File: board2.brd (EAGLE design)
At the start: 100 x 80 mm, 76 parts, among them Q1 7.68M, Q2 16MHz

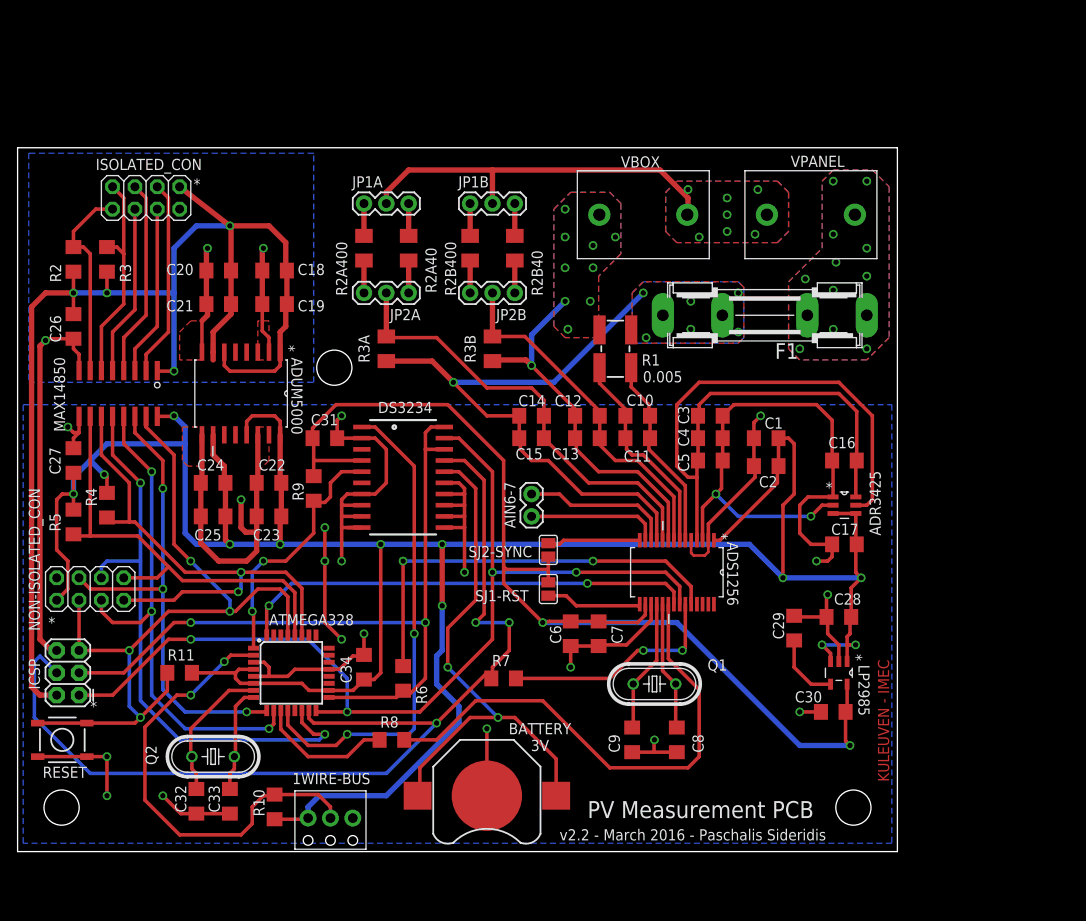
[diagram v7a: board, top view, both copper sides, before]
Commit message: Visual changes and clean up
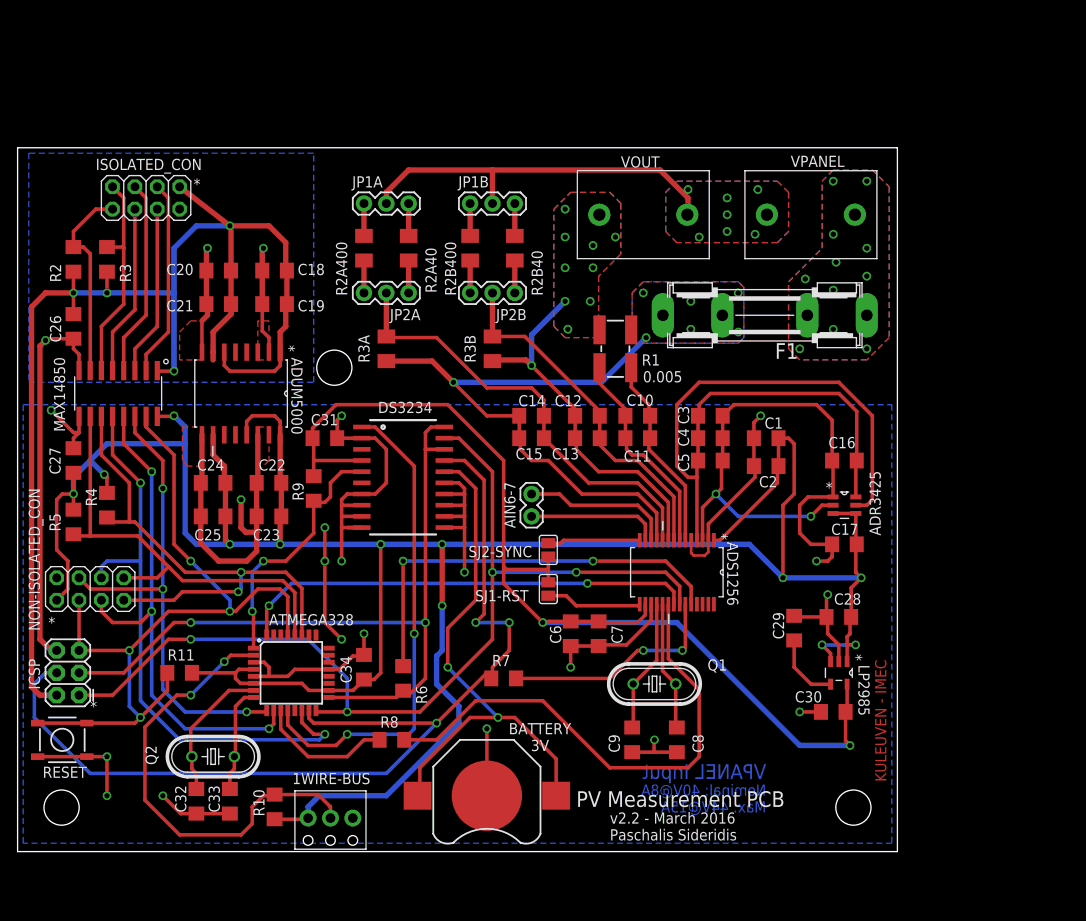
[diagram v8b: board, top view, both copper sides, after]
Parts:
- renumbered VBOX to VOUT
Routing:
- net MOSI: track 118.2 -> 115.2 mm
- net GND_ISO: track 269.9 -> 272.6 mm
- net AIN5: track 68.9 -> 67.2 mm
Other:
- board text added: "Nominal: 40V@8A Max: 44V@15A"
- board text added: "VPANEL Input"
- board text added: "v2.2 - March 2016 Paschalis Sideridis"
- board text removed: "v2.2 - March 2016 - Paschalis Sideridis"
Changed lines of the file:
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@@
 <wire x1="100" y1="80" x2="0" y2="80" width="0" layer="20"/>
 <wire x1="0" y1="80" x2="0" y2="0" width="0" layer="20"/>
-<text x="64.77" y="3.81" size="1.9304" layer="112">PV Measurement PCB</text>
+<text x="63.5" y="5.08" size="1.778" layer="112" font="vector">PV Measurement PCB</text>
 <hole x="5" y="5" drill="4"/>
 <hole x="95" y="5" drill="4"/>
 <hole x="36" y="55" drill="4"/>
-<text x="99.06" y="7.9375" size="1.27" layer="1" rot="R90">KULEUVEN - IMEC</text>
-<text x="61.595" y="1.27" size="1.27" layer="112">v2.2 - March 2016 - Paschalis Sideridis</text>
+<text x="98.7425" y="7.9375" size="1.27" layer="1" font="vector" rot="R90">KULEUVEN - IMEC</text>
+<text x="67.31" y="1.27" size="1.27" layer="112" font="vector">v2.2 - March 2016
+Paschalis Sideridis</text>
 <text x="59.3725" y="14.605" size="1.27" layer="112" rot="R180" align="bottom-center">BATTERY
 3V</text>
@@
 <text x="3.4925" y="25.4" size="1.27" layer="112">*</text>
 <text x="8.255" y="15.875" size="1.27" layer="112">*</text>
+<text x="85.09" y="8.255" size="1.6764" layer="16" font="vector" rot="MR0">VPANEL Input</text>
+<text x="85.09" y="4.445" size="1.27" layer="16" font="vector" rot="MR0">Nominal: 40V@8A
+Max: 44V@15A</text>
+<polygon width="0.4064" layer="42">
+<vertex x="67.31" y="10.16"/>
+<vertex x="85.725" y="10.16"/>
+<vertex x="85.725" y="3.175"/>
+<vertex x="67.31" y="3.175"/>
+</polygon>
 </plain>
 <attributes>
@@
 <attribute name="VALUE" x="19.685" y="78.74" size="1.27" layer="27" rot="R180"/>
 </element>
-<element name="VBOX" library="TE CONNECTIVITY" package="2TERMINALBLOCK_10MMPITCH" value="2PIN_TERMINAL_PCBMOUNT" x="71.12" y="72.39" smashed="yes">
+<element name="VOUT" library="TE CONNECTIVITY" package="2TERMINALBLOCK_10MMPITCH" value="2PIN_TERMINAL_PCBMOUNT" x="71.12" y="72.39" smashed="yes">
 <attribute name="NAME" x="68.565" y="77.755" size="1.27" layer="25"/>
 </element>
@@
 <signal name="VBUS1">
 <contactref element="VPANEL" pad="1"/>
-<contactref element="VBOX" pad="1"/>
+<contactref element="VOUT" pad="1"/>
 <contactref element="JP1A" pad="2"/>
 <contactref element="JP1B" pad="2"/>
@@
 </signal>
 <signal name="AIN3">
-<contactref element="VBOX" pad="2"/>
+<contactref element="VOUT" pad="2"/>
 <contactref element="R1" pad="OUTI"/>
 <contactref element="R3B" pad="1"/>
@@
 <via x="76.5175" y="59.3725" extent="1-16" drill="0.6"/>
 <via x="71.12" y="63.5" extent="1-16" drill="0.6"/>
-<wire x1="49.53" y1="53.34" x2="60.96" y2="53.34" width="0.6096" layer="16"/>
-<wire x1="60.96" y1="53.34" x2="71.12" y2="63.5" width="0.6096" layer="16"/>
+<wire x1="49.53" y1="53.34" x2="66.3575" y2="53.34" width="0.6096" layer="16"/>
 <wire x1="41.91" y1="55.75" x2="47.12" y2="55.75" width="0.6096" layer="1"/>
+<wire x1="66.3575" y1="53.34" x2="71.4375" y2="58.42" width="0.6096" layer="16"/>
 </signal>
 <signal name="VBUS2">
@@
 <contactref element="R3" pad="1"/>
 <contactref element="ISOLATED_CON" pad="7"/>
-<wire x1="10.16" y1="68.71" x2="11.3" y2="68.71" width="0.4064" layer="1"/>
-<wire x1="11.3" y1="68.71" x2="12.065" y2="67.945" width="0.4064" layer="1"/>
-<wire x1="12.065" y1="67.945" x2="12.065" y2="62.23" width="0.4064" layer="1"/>
 <wire x1="12.065" y1="62.23" x2="9.525" y2="59.69" width="0.4064" layer="1"/>
 <wire x1="9.525" y1="59.69" x2="9.525" y2="54.67" width="0.4064" layer="1"/>
 <wire x1="10.795" y1="75.565" x2="12.065" y2="74.295" width="0.4064" layer="1"/>
-<wire x1="12.065" y1="74.295" x2="12.065" y2="67.945" width="0.4064" layer="1"/>
+<wire x1="12.065" y1="74.295" x2="12.065" y2="68.58" width="0.4064" layer="1"/>
+<wire x1="12.065" y1="68.58" x2="12.065" y2="62.23" width="0.4064" layer="1"/>
+<wire x1="10.16" y1="68.71" x2="11.935" y2="68.71" width="0.4064" layer="1"/>
+<wire x1="11.935" y1="68.71" x2="12.065" y2="68.58" width="0.4064" layer="1"/>
 </signal>
 <signal name="SCL">
@@
 <vertex x="27.305" y="43.18"/>
 </polygon>
-<wire x1="6.985" y1="47.625" x2="6.35" y2="47.625" width="0.4064" layer="1"/>
-<wire x1="6.35" y1="47.625" x2="5.715" y2="48.26" width="0.4064" layer="1"/>
-<via x="5.715" y="48.26" extent="1-16" drill="0.6"/>
+<via x="3.81" y="50.165" extent="1-16" drill="0.6"/>
 <wire x1="34.925" y1="36.83" x2="34.925" y2="33.02" width="0.4064" layer="1"/>
 <via x="34.925" y="36.83" extent="1-16" drill="0.6"/>
@@
 <wire x1="20.32" y1="4.315" x2="18.545" y2="4.315" width="0.4064" layer="1"/>
 <wire x1="18.545" y1="4.315" x2="16.51" y2="6.35" width="0.4064" layer="1"/>
+<wire x1="6.985" y1="47.625" x2="6.35" y2="47.625" width="0.4064" layer="1"/>
+<wire x1="6.35" y1="47.625" x2="3.81" y2="50.165" width="0.4064" layer="1"/>
 </signal>
 <signal name="IN2_ISO">
@@
 <wire x1="53.0225" y1="26.9875" x2="52.07" y2="26.035" width="0.4064" layer="1"/>
 <wire x1="8.255" y1="8.89" x2="1.905" y2="15.24" width="0.4064" layer="16"/>
-<wire x1="1.905" y1="15.24" x2="1.905" y2="21.59" width="0.4064" layer="16"/>
-<wire x1="1.905" y1="21.59" x2="2.54" y2="22.225" width="0.4064" layer="16"/>
-<wire x1="2.54" y1="22.225" x2="4.445" y2="20.32" width="0.4064" layer="16"/>
+<wire x1="1.905" y1="15.24" x2="1.905" y2="19.05" width="0.4064" layer="16"/>
+<wire x1="1.905" y1="19.05" x2="3.175" y2="20.32" width="0.4064" layer="16"/>
+<wire x1="3.175" y1="20.32" x2="4.445" y2="20.32" width="0.4064" layer="16"/>
 </signal>
 <signal name="RTC_CS">
